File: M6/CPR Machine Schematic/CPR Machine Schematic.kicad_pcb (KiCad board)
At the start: 2 copper layers, 134 x 94 mm, 67 parts, among them J1 Contactor 22.2V IN, J10 Stop Button Port, J11 Go Button Port, J12 I2C Port, J13 Raspberry_Pi_2_3, J2 5V Spare Headers, J3 Power Switch, J4 3V3 Spare Headers, J5 12 Spare headers, J6 Battery Spare headers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

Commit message: finished PCB Draft
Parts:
- added F1: 5A, Fuse:Fuse_1206_3216Metric, F.Cu at (133.9, 111.7)
- added REF**: MountingHole_2.7mm_Pad, MountingHole:MountingHole_2.7mm_Pad, F.Cu at (118.6, 76.0)
- added REF**: MountingHole_2.7mm_Pad, MountingHole:MountingHole_2.7mm_Pad, F.Cu at (176.6, 125.0)
- added REF**: Untitled, MAX42402AFLB_:Untitled, F.Cu at (169.5, 104.2)
- added REF**: MountingHole_2.7mm_Pad, MountingHole:MountingHole_2.7mm_Pad, F.Cu at (118.6, 125.0)
- added REF**: MountingHole_2.7mm_Pad, MountingHole:MountingHole_2.7mm_Pad, F.Cu at (176.6, 76.0)
- C8, J13: moved to B.Cu
- F2: value 4A -> 3A; moved to B.Cu
- Q2: value DMG2305UX-13 MOSFET -> AO3407A; footprint 2679:SOT91P240X110-3N -> Package_TO_SOT_SMD:SOT-23-3
- moved J12 136.7 mm to (185.1, 123.7)
- moved J8 121.8 mm to (189.8, 118.0)
- moved J11 120.3 mm to (185.1, 94.5)
- moved J10 120.0 mm to (185.1, 107.1)
- moved R15 113.1 mm to (181.1, 96.0), turned to 90 degrees
- moved R5 111.3 mm to (181.1, 105.0), turned to 90 degrees
- moved Q7 107.9 mm to (177.0, 99.0), turned to -90 degrees
- moved Q3 105.8 mm to (177.0, 106.4), turned to -90 degrees
- moved J6 105.5 mm to (164.1, 77.8), turned to 90 degrees
- moved J5 103.4 mm to (158.0, 77.8), turned to 90 degrees
- moved C13 94.3 mm to (169.9, 112.5), turned to 180 degrees
- moved R16 91.4 mm to (169.9, 110.1), turned to 0 degrees
- moved U3 89.6 mm to (170.9, 116.7), turned to 0 degrees
- moved C_OPT1 88.1 mm to (167.5, 116.9), turned to 90 degrees
- moved J4 88.0 mm to (149.3, 77.8), turned to 90 degrees
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- renumbered TP2 to 12V, TP4 to 3V3, TP3 to 5V, TP1 to Batt
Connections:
- net /HMI_Raspi/Go_Button renamed /HMI_Raspi/Go Button
- net /HMI_Raspi/Stop_Button renamed /HMI_Raspi/Stop Button
- net Net-(J10-Pin_1) renamed /HMI_Raspi/Stop Button Ground
- net Net-(J10-Pin_3) renamed /HMI_Raspi/Stop LED Power
- net Net-(J11-Pin_1) renamed /HMI_Raspi/Go Button Ground
- net Net-(J11-Pin_3) renamed /HMI_Raspi/Go LED Power
- C8 pad 1: Net-(U2-GND) -> GND
- F2 pad 1: Net-(F2-Pad1) -> +5V
- J1 pad 1: +22.2V -> /Power/Contactor +
- J3 pad 1: Net-(J3-Pin_1) -> /Power/To Contactor
- J3 pad 2: Net-(J3-Pin_2) -> /Power/From Switch
- Q2 pad 2: Net-(F2-Pad1) -> Net-(F1-Pad1)
- Q2 pad 3: +5V -> /Power/Contactor +
- Q4 pad 5: Net-(F2-Pad1) -> Net-(F1-Pad1)
- Q4 pad 6: +5V -> /Power/Contactor +
- U2 pad 11: Net-(C6-Pad2) -> Net-(U2-BIAS)
- U2 pad 12: unconnected-(U2-NC-Pad12) -> Net-(U2-BIAS)
- U2 pad 13: Net-(U2-BST) -> Net-(U2-FB)
- U2 pad 14: Net-(U2-GND) -> Net-(U2-PGOOD)
- U2 pad 8: GND -> unconnected-(U2-NC-Pad8)
- U2 pad 9: Net-(U2-LX) -> Net-(U2-BST)
- U4 pad 1: Net-(J3-Pin_1) -> /Power/From Switch
- U4 pad 3: Net-(J3-Pin_2) -> /Power/To Contactor
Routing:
- net +12V: track 0.00 -> 132.3 mm, vias 0 -> 8
- net +22.2V: track 2.54 -> 114.6 mm, vias 0 -> 1
- net /HMI_Raspi/Go Button: track 0.00 -> 76.5 mm, vias 0 -> 1
- net GND: track 3.70 -> 67.6 mm, vias 1 -> 8
- net /HMI_Raspi/Stop Button: track 0.00 -> 56.3 mm, vias 0 -> 1
- net /HMI_Raspi/Go_Enable: track 0.00 -> 56.2 mm
- net /Raspi/I2C_SDA: track 17.0 -> 62.8 mm
- net +3.3V: track 18.7 -> 64.5 mm, vias 0 -> 1
- net /Raspi/I2C_SCL: track 19.6 -> 61.0 mm
- net /HMI_Raspi/Laser_PWM: track 18.7 -> 47.1 mm, vias 0 -> 2
- net /HMI_Raspi/Stop_Enable: track 0.00 -> 25.2 mm
- net +5V: track 10.2 -> 33.0 mm, vias 0 -> 13
- net Net-(D3-K): track 0.00 -> 18.8 mm, vias 0 -> 4
- net Net-(D2-K): track 0.00 -> 18.4 mm
- net Net-(U2-FB): track 0.00 -> 18.4 mm, vias 0 -> 4
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- added copper zone on B.Cu, net +5V
- added copper zone on F.Cu, net GND
- removed copper zone on F.Cu, net +5V
- removed copper zone on B.Cu, net GND
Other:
- board size 134 x 94 mm -> 79.8 x 56.2 mm
- board text added: "12V"
- board text added: "12V - 5V Buck"
- board text added: "3V3"
- board text added: "5V"
- board text added: "BATT"
- board text added: "Battery - 12V Buck"
- board text added: "CT"
- board text added: "CT+"
- board text added: "CT-"
- board text added: "Daniel Gliksberg HB Main Board v1 2.679"
- board text added: "Force +"
- board text added: "Force -"
- board text added: "Force Amp"
- board text added: "GND"
- board text added: "Go GND"
- board text added: "Go Pwr"
- board text added: "Go Sig"
- board text added: "Laser +"
- board text added: "Laser -"
- board text added: "OV Diode"
- board text added: "SCL"
- board text added: "SDA"
- board text added: "SW"
- board text added: "Stop GND"
- board text added: "Stop Pwr"
- board text added: "Stop Sig"

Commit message: PCB Feedback V1
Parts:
- added R17: 90 kOhm, Resistor_SMD:R_1206_3216Metric, B.Cu at (166.4, 117.2)
- added R18: 10 kOhm, Resistor_SMD:R_1206_3216Metric, B.Cu at (164.1, 117.2)
- added R19: 10 kOhm, Resistor_SMD:R_1206_3216Metric, F.Cu at (178.1, 85.5)
- added R20: 10 kOhm, Resistor_SMD:R_1206_3216Metric, B.Cu at (177.2, 109.0)
- added R21: 10 kOhm, Resistor_SMD:R_1206_3216Metric, B.Cu at (177.3, 101.2)
- added R22: 100 Ohm, Resistor_SMD:R_1206_3216Metric, B.Cu at (177.2, 106.5)
- added R23: 100 Ohm, Resistor_SMD:R_1206_3216Metric, B.Cu at (177.3, 98.5)
- added R24: 100 Ohm, Resistor_SMD:R_1206_3216Metric, F.Cu at (175.8, 85.5)
- added U5: MCP3021A0T-E_OT, 2679:IC_MCP3021A0T-E_OT, F.Cu at (178.2, 118.8)
- R11: value 193 Ohm -> 220 Ohm
- R12: value 80 Ohm -> 100 Ohm
- R16: value 10 kOhm -> 80 Ohm
- U3: value MCP6001R -> MCP6004; footprint Package_TO_SOT_SMD:SOT-23-5 -> MCP6004:SOIC14_SL_MCH
- moved REF** 24.3 mm to (173.2, 80.2)
- moved C_OPT1 10.8 mm to (178.2, 115.8), turned to 180 degrees
- moved R16 5.51 mm to (169.9, 104.6)
- moved C13 5.51 mm to (169.9, 107.0)
- moved R6 4.73 mm to (181.4, 85.5)
- moved U3 3.61 mm to (169.1, 113.5)
- renumbered Batt to TP1, 12V to TP2, 5V to TP3, 3V3 to TP4
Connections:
- C13 pad 2: /Raspi/FORCE_IN -> Net-(U5-AIN)
- C_OPT1 pad 2: /Raspi/FORCE_IN -> Net-(U5-AIN)
- J13 pad 15: /Raspi/FORCE_IN -> unconnected-(J13-GPIO22-Pad15)
- J9 pad 1: GND -> Net-(J9-Pin_1)
- Q3 pad 4: /HMI_Raspi/Stop_Enable -> Net-(Q3-G)
- Q6 pad 1: Net-(Q6-S-Pad1) -> GND
- Q6 pad 2: Net-(Q6-S-Pad1) -> GND
- Q6 pad 3: Net-(Q6-S-Pad1) -> GND
- Q6 pad 4: /HMI_Raspi/Laser_PWM -> Net-(Q6-G)
- Q6 pad 5: +5V -> Net-(J9-Pin_1)
- Q7 pad 4: /HMI_Raspi/Go_Enable -> Net-(Q7-G)
- R16 pad 1: /Raspi/FORCE_IN -> Net-(U5-AIN)
- R6 pad 2: Net-(Q6-S-Pad1) -> +5V
- U3 pad 1: /Raspi/FORCE_IN -> Net-(U5-AIN)
- U3 pad 2: +5V -> Net-(J8-Pin_1)
- U3 pad 3: GND -> /Sensing/Vref
- U3 pad 4: Net-(J8-Pin_1) -> +5V
- U3 pad 5: GND -> (no net)
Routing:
- net /Raspi/FORCE_IN: track 40.5 -> 0.00 mm
- net Net-(U5-AIN): track 0.00 -> 28.3 mm, vias 0 -> 4
- net GND: track 67.6 -> 89.8 mm, vias 8 -> 9
- net Net-(J9-Pin_1): track 0.00 -> 16.3 mm
- net /HMI_Raspi/Laser_PWM: track 47.1 -> 56.3 mm
- net /Sensing/Vref: track 0.00 -> 8.00 mm, vias 0 -> 1
- net Net-(Q6-S-Pad1): track 6.80 -> 0.00 mm
- net Net-(Q7-G): track 0.00 -> 6.40 mm, vias 0 -> 1
- net /Raspi/I2C_SCL: track 61.0 -> 66.9 mm, vias 0 -> 1
- net Net-(J9-Pin_2): track 10.9 -> 6.59 mm
- net /Raspi/I2C_SDA: track 62.8 -> 67.0 mm, vias 0 -> 1
- net Net-(Q3-G): track 0.00 -> 4.03 mm, vias 0 -> 1
- net Net-(J8-Pin_1): track 28.0 -> 31.9 mm, vias 2 -> 0
- net Net-(Q6-G): track 0.00 -> 1.97 mm
- net +5V: track 33.0 -> 34.9 mm, vias 13 -> 15
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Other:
- board text added: "ADC"
- board text added: "Batt"
- board text added: "Force In"
- board text removed: "Force +"
- board text removed: "Force -"

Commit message: PCB V2 Part 2
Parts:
- C1, C10, C11, C12, C13, C3, C4, C5, C6, C7, C8, C9, C_OPT1: footprint Capacitor_SMD:C_1206_3216Metric -> Capacitor_SMD:C_1206_3216Metric_Pad1.33x1.80mm_HandSolder
- C2: footprint Capacitor_SMD:C_1206_3216Metric -> Capacitor_THT:CP_Radial_D10.0mm_P5.00mm
- D2: value B220 -> B220a; footprint Diode_SMD:D_SMB -> Diode_SMD:D_SMA_Handsoldering
- D3: footprint Diode_SMD:D_SMA -> Diode_SMD:D_SMB_Handsoldering
- F1, F2: footprint Fuse:Fuse_1206_3216Metric -> Fuse:Fuse_1206_3216Metric_Pad1.42x1.75mm_HandSolder
- L2: value 5 uH -> 6.8 uH
- Q1: footprint Package_TO_SOT_THT:TO-92_Inline -> Package_TO_SOT_THT:TO-92_Inline_Wide
- Q3, Q6, Q7: value FDMS8350LET40 -> T2N7002BK,LM; footprint Package_TO_SOT_SMD:TDSON-8-1 -> Package_TO_SOT_SMD:SOT-23_Handsoldering
- R1, R4: value 50 kOhm -> 49.9 kOhm; footprint Resistor_SMD:R_1206_3216Metric -> Resistor_SMD:R_1206_3216Metric_Pad1.30x1.75mm_HandSolder
- R10: value 660 Ohm -> 665 Ohm; footprint Resistor_SMD:R_1206_3216Metric -> Resistor_SMD:R_1206_3216Metric_Pad1.30x1.75mm_HandSolder
- R11, R12, R13, R14, R17, R18, R19, R2, R20, R21, R22, R23, R24, R3, R7, R8: footprint Resistor_SMD:R_1206_3216Metric -> Resistor_SMD:R_1206_3216Metric_Pad1.30x1.75mm_HandSolder
- R15, R5: value 50 Ohm -> 49.9 Ohm; footprint Resistor_SMD:R_1206_3216Metric -> Resistor_SMD:R_1206_3216Metric_Pad1.30x1.75mm_HandSolder
- R16: value 80 Ohm -> 80.6 Ohm; footprint Resistor_SMD:R_1206_3216Metric -> Resistor_SMD:R_1206_3216Metric_Pad1.30x1.75mm_HandSolder
- R9: value 1.4 kOhm -> 1.5 kOhm; footprint Resistor_SMD:R_1206_3216Metric -> Resistor_SMD:R_1206_3216Metric_Pad1.30x1.75mm_HandSolder
- moved REF** 25.0 mm to (161.9, 102.5)
- moved C2 5.44 mm to (152.2, 103.2), turned to 90 degrees
- moved C6 3.81 mm to (146.4, 105.7)
- moved C7 3.81 mm to (144.1, 105.7)
- moved R2 3.81 mm to (141.7, 105.7)
- moved C3 3.51 mm to (138.1, 105.0)
- moved R1 3.51 mm to (138.1, 102.5)
- moved L1 2.78 mm to (158.0, 112.0)
- moved R5 2.53 mm to (181.0, 107.5)
- moved Q6 2.33 mm to (178.7, 90.0), turned to 0 degrees
- moved R15 2.28 mm to (181.0, 98.2)
- moved R8 1.75 mm to (146.6, 84.2)
- moved C1 1.48 mm to (147.8, 109.5)
- moved C9 1.25 mm to (152.8, 94.0), turned to 0 degrees
- moved Q3 1.16 mm to (176.8, 107.5)
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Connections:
- Q3 pad 1: GND -> Net-(Q3-S-Pad1)
- Q3 pad 3: GND -> /HMI_Raspi/Stop Button Ground
- Q6 pad 1: GND -> Net-(Q6-G)
- Q6 pad 3: GND -> Net-(J9-Pin_1)
- Q7 pad 1: GND -> Net-(Q7-S-Pad1)
- Q7 pad 3: GND -> /HMI_Raspi/Go Button Ground
- R22 pad 2: Net-(Q3-G) -> Net-(Q3-S-Pad1)
- R23 pad 2: Net-(Q7-G) -> Net-(Q7-S-Pad1)
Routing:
- net GND: track 89.8 -> 79.5 mm
- net +12V: track 132.3 -> 122.3 mm, vias 8 -> 4
- net Net-(Q7-G): track 6.40 -> 0.00 mm, vias 1 -> 0
- net Net-(J9-Pin_1): track 16.3 -> 9.98 mm
- net Net-(Q3-S-Pad1): track 0.00 -> 4.67 mm, vias 0 -> 1
- net Net-(Q3-G): track 4.03 -> 0.00 mm, vias 1 -> 0
- net Net-(U1-~SHDN): track 14.0 -> 17.9 mm
- net /HMI_Raspi/Go LED Power: track 9.66 -> 12.4 mm
- net Net-(Q7-S-Pad1): track 0.00 -> 2.63 mm, vias 0 -> 1
- net Net-(U2-FB): track 18.4 -> 20.9 mm, vias 4 -> 2
- net /HMI_Raspi/Stop LED Power: track 6.27 -> 8.79 mm
- net /HMI_Raspi/Go Button Ground: track 13.6 -> 15.6 mm
- net Net-(Q1-C): track 14.4 -> 16.2 mm
- net Net-(Q1-B): track 8.18 -> 9.72 mm
- net +5V: track 34.9 -> 33.8 mm, vias 15 -> 14
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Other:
- board text added: "Go Button"
- board text added: "I2C"
- board text added: "Stop Button"

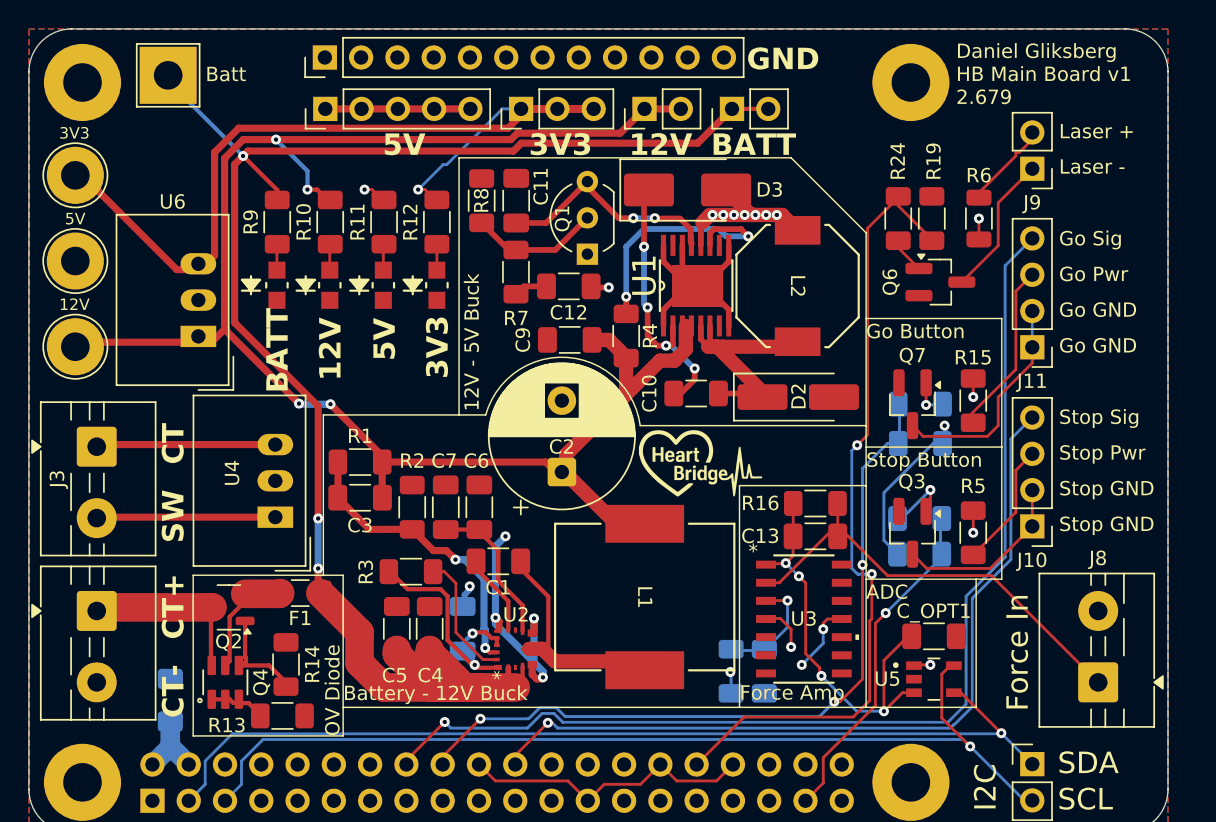
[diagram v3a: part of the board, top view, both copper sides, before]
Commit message: Down with the second buck converter
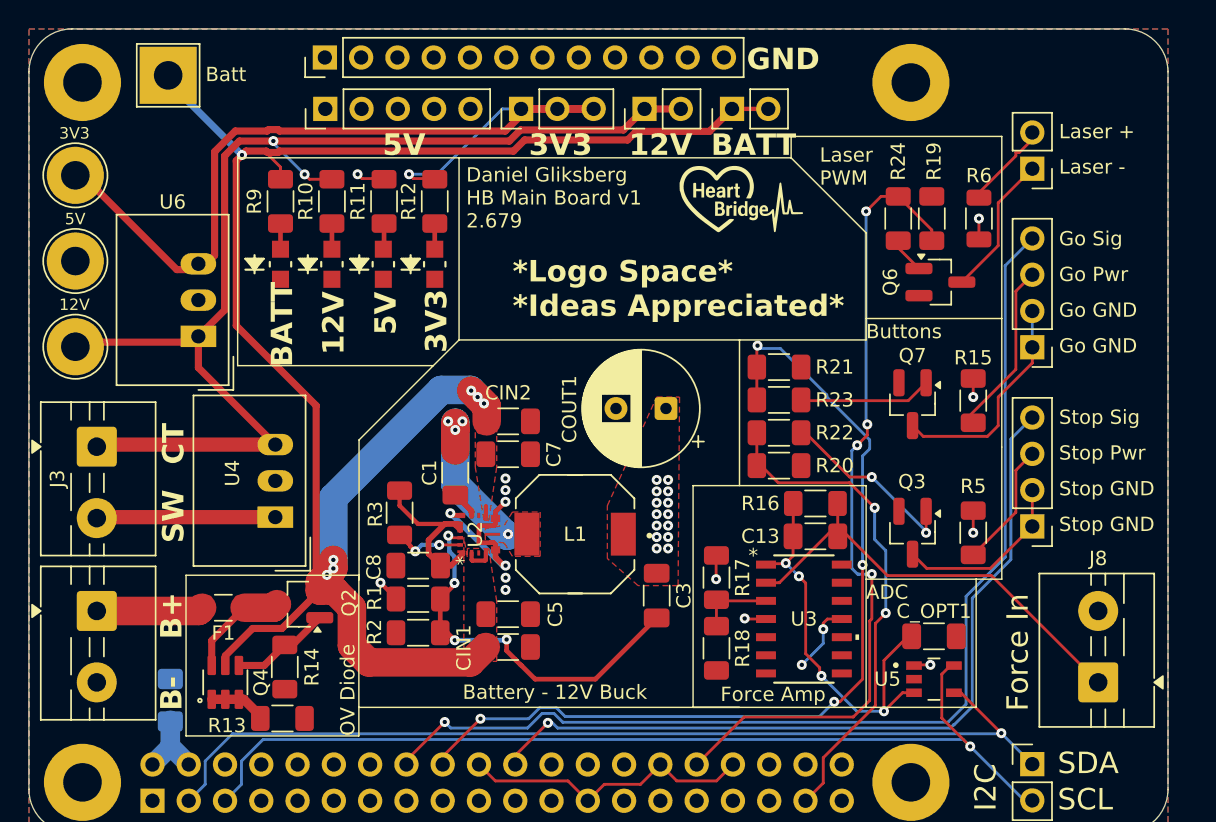
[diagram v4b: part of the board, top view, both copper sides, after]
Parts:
- removed C10: 0.18 uF, Capacitor_SMD:C_1206_3216Metric_Pad1.33x1.80mm_HandSolder
- removed C11: 330 pF, Capacitor_SMD:C_1206_3216Metric_Pad1.33x1.80mm_HandSolder
- removed C12: 15 nF, Capacitor_SMD:C_1206_3216Metric_Pad1.33x1.80mm_HandSolder
- removed C9: 2.2 uF, Capacitor_SMD:C_1206_3216Metric_Pad1.33x1.80mm_HandSolder
- removed D2: B220a, Diode_SMD:D_SMA_Handsoldering
- removed D3: SS24, Diode_SMD:D_SMB_Handsoldering
- removed L2: 6.8 uH, SRU8043_6R8Y:IND_BOURNS_SRU8043
- removed Q1: 2N3904, Package_TO_SOT_THT:TO-92_Inline_Wide
- removed R4: 49.9 kOhm, Resistor_SMD:R_1206_3216Metric_Pad1.30x1.75mm_HandSolder
- removed R7: 2 kOhm, Resistor_SMD:R_1206_3216Metric_Pad1.30x1.75mm_HandSolder
- removed R8: 47 kOhm, Resistor_SMD:R_1206_3216Metric_Pad1.30x1.75mm_HandSolder
- removed U1: LT1765EFE-5_PBF, LT1765EFE_5_PBF:SOP65P640X110-17N
- added REF**: Angy, Images:Angy, B.Cu at (157.3, 88.5)
- C3: value 22 pF -> 47 pF
- C8, R17, R18, R20, R21, R22, R23: moved to F.Cu
- COUT1: renamed from C2; value 50 uF -> 47 uF; footprint Capacitor_THT:CP_Radial_D10.0mm_P5.00mm -> Capacitor_THT:CP_Radial_D8.0mm_P3.50mm
- J1: value Contactor 22.2V IN -> Battery 22.2V IN
- L1: value 12 uH -> 2.2 uH; footprint DR124_120_R:IND_CB_DR124 -> Imports:IND_1217AS-H-2R2N=P3
- Q2: footprint Package_TO_SOT_SMD:SOT-23-3 -> Package_TO_SOT_SMD:SOT-23_Handsoldering
- R2: value 3.57 kOhm -> 9.5 kOhm
- U2: value MAX42402AFLB+ -> MAX42403AFLB+
- moved C3 21.9 mm to (158.8, 111.9), turned to 90 degrees
- moved REF** 18.7 mm to (164.8, 84.0)
- moved R20 11.6 mm to (167.4, 102.8), turned to 0 degrees
- moved R22 11.5 mm to (167.4, 100.5), turned to 0 degrees
- moved R21 11.3 mm to (167.4, 95.9)
- moved R1 10.4 mm to (142.1, 112.1), turned to 0 degrees
- moved R23 9.90 mm to (167.4, 98.2)
- moved R2 8.80 mm to (142.1, 114.5), turned to 180 degrees
- moved COUT1 8.54 mm to (159.5, 98.8), turned to 180 degrees
- moved U2 8.43 mm to (146.4, 107.6)
- moved C5 7.86 mm to (148.4, 113.2), turned to 180 degrees
- moved R17 7.37 mm to (163.0, 110.6), turned to -90 degrees
- moved C1 6.89 mm to (144.7, 103.3), turned to -90 degrees
- moved L1 6.57 mm to (153.1, 107.6), turned to 180 degrees
- moved CIN2 6.34 mm to (148.4, 99.7), turned to 180 degrees
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- renumbered C4 to CIN1, C6 to CIN2
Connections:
- net Net-(U2-BST) renamed /Power/BST
- net Net-(U2-LX) renamed /Power/LX
- C3 pad 2: +12V -> +5V
- C7 pad 2: Net-(C6-Pad2) -> +22.2V
- CIN2 pad 2: Net-(C6-Pad2) -> +22.2V
- COUT1 pad 1: +12V -> +5V
- F1 pad 1: Net-(F1-Pad1) -> /Power/Battery +
- F1 pad 2: +22.2V -> Net-(F1-Pad2)
- J1 pad 1: /Power/Contactor + -> /Power/Battery +
- J3 pad 1: /Power/To Contactor -> +12V
- L1 pad 1: +12V -> +5V
- Q2 pad 2: Net-(F1-Pad1) -> +22.2V
- Q2 pad 3: /Power/Contactor + -> Net-(F1-Pad2)
- Q4 pad 5: Net-(F1-Pad1) -> +22.2V
- Q4 pad 6: /Power/Contactor + -> Net-(F1-Pad2)
- R1 pad 1: +12V -> +5V
- U2 pad 7: Net-(C6-Pad2) -> +22.2V
- U4 pad 3: /Power/To Contactor -> +12V
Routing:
- net GND: track 79.5 -> 39.1 mm
- net +12V: track 122.3 -> 83.3 mm, vias 4 -> 2
- net +5V: track 33.8 -> 12.2 mm, vias 14 -> 22
- net Net-(D3-K): track 18.7 -> 0.00 mm, vias 4 -> 0
- net Net-(D2-K): track 18.4 -> 0.00 mm
- net +22.2V: track 114.8 -> 133.2 mm, vias 3 -> 7
- net Net-(U1-~SHDN): track 17.9 -> 0.00 mm, vias 2 -> 0
- net Net-(Q1-C): track 16.2 -> 0.00 mm, vias 2 -> 0
- net /Power/To Contactor: track 12.6 -> 0.00 mm
- net /Power/Contactor +: track 12.4 -> 0.00 mm
- net /HMI_Raspi/Stop_Enable: track 23.7 -> 34.9 mm, vias 1 -> 2
- net /HMI_Raspi/Go_Enable: track 53.5 -> 64.4 mm, vias 3 -> 4
- net Net-(C6-Pad2): track 10.7 -> 0.00 mm
- net Net-(Q1-B): track 9.72 -> 0.00 mm
- net Net-(Q3-G): track 4.67 -> 13.2 mm, vias 1 -> 2
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- added copper zone on F.Cu, net +22.2V
- added copper zone on F.Cu, net +5V
- added copper zone on F.Cu, net /Power/LX
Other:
- board text added: "*Logo Space* *Ideas Appreciated*"
- board text added: "B+"
- board text added: "B-"
- board text added: "Buttons"
- board text added: "Laser PWM"
- board text removed: "12V - 5V Buck"
- board text removed: "CT+"
- board text removed: "CT-"
- board text removed: "Go Button"
- board text removed: "Stop Button"

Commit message: lil guy icon
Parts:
- added G***: LOGO, Images:LilGuy, F.Cu at (190.6, 76.0)
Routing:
- net Net-(U2-BIAS): track 13.5 -> 11.7 mm
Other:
- board size 79.8 x 56.2 mm -> 79.8 x 56.3 mm
